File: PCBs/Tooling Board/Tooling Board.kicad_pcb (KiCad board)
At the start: 2 copper layers, 106 parts, among them J101 Screw Terminal, J102 Screw Terminal, J103 USB_B_Mini, J201 Conn_02x05_Odd_Even, J301 Conn_01x02, J302 Conn_01x02, J401 Screw Terminal, J402 Screw Terminal, J403 Screw Terminal, J404 Screw Terminal, J501 Screw Terminal, J502 Screw Terminal, J503 Screw Terminal, J504 Screw Terminal, J601 Screw Terminal, J602 Screw Terminal, J603 Screw Terminal, J604 Screw Terminal, J701 Conn_01x03, J702 Conn_01x04, J703 Conn_01x03, J801 Conn_01x02, Q301 Q_NMOS_DGS, Q302 Q_NMOS_DGS, SW201 SW_Push, U101 TLV733P, U201 ATSAMD21E18A-MFTCT-ND, U401 74LVC2G14, U402 LN298P, U501 74LVC2G14, U502 LN298P, U601 74LVC2G14, U602 LN298P, U701 ADA_IMU, U801 CA3140AM, U802 LM2776, U803 TL081BCDG4, Y201 32.7680kHz

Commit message: Removed 3rd DC Motor Driver
-Can only do 4 DC motors now, not enough board space
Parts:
- removed C601, C602: 100nF, Capacitors_SMD:C_0805_HandSoldering
- removed J601, J602, J603, J604: Screw Terminal, EER:RingTerminal
- removed R601, R602: 0.5, Resistors_SMD:R_1206_HandSoldering
- removed U601: 74LVC2G14, EER:PSON50P140X100X40-6N
- removed U602: LN298P, EER:POWER-SO20
- RV801: footprint Potentiometers:Potentiometer_Trimmer_Bourns_3269W -> Potentiometers:Potentiometer_Trimmer_Bourns_3296W
- moved J403 297.6 mm to (159.6, 47.4), turned to 90 degrees
- moved J404 297.6 mm to (159.6, 38.0), turned to 90 degrees
- moved U802 285.1 mm to (159.6, 97.0)
- moved J402 274.4 mm to (144.6, 38.0), turned to 90 degrees
- moved J401 274.2 mm to (144.4, 47.2), turned to 90 degrees
- moved U803 252.4 mm to (198.2, 69.4)
- moved SW201 252.0 mm to (145.8, 87.8), turned to 90 degrees
- moved Q302 249.9 mm to (188.0, 71.4)
- moved U801 249.4 mm to (197.6, 78.6)
- moved U201 244.1 mm to (149.5, 77.7)
- moved J201 242.2 mm to (151.2, 90.4), turned to 180 degrees
- moved Q301 217.9 mm to (158.4, 71.4)
- moved J502 210.4 mm to (133.2, 37.8), turned to 90 degrees
- moved J504 203.3 mm to (133.0, 47.0), turned to 90 degrees
- moved J102 202.4 mm to (132.4, 78.2), turned to 90 degrees
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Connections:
- U201 pad 25: DirA3 -> Net-(U201-Pad25)
- U201 pad 3: DirB3 -> Net-(U201-Pad3)
- U201 pad 7: EnableA3 -> Net-(U201-Pad7)
- U201 pad 8: EnableB3 -> Net-(U201-Pad8)
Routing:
- net (no net): vias 0 -> 3
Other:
- board outline added: 104.7 x 67.4 mm

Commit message: Almost Finished
-Still going, help
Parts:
- removed D801: GREEN, LEDs:LED_0805_HandSoldering
- removed R301, R302: 100k, Resistors_SMD:R_0805_HandSoldering
- removed R809: 1k, Resistors_SMD:R_0805_HandSoldering
- C103, C105, C106, C107, C201, C202, C203, C204, C207, C401, C402, C501, C502, C701, C801, C802, C803, C804, C805, C806, C807, C808, C809, C810, C811, C812, C813: footprint Capacitors_SMD:C_0805_HandSoldering -> Capacitors_SMD:C_0805
- C205, C206: footprint Capacitors_SMD:C_0603_HandSoldering -> Capacitors_SMD:C_0603
- D101, D201, D202: footprint LEDs:LED_0805_HandSoldering -> LEDs:LED_0805
- J301, J302, J801: footprint Junction Box:70553-02 -> EER:1x2_molex_llc_new
- J701, J703: footprint Junction Box:70553-03 -> EER:1x3_molex_llc
- J702: footprint Junction Box:70553-04 -> EER:1x4_molex_llc
- R101, R201, R202, R203, R204, R205, R701, R702, R703, R801, R802, R803, R804, R805, R806, R807, R808: footprint Resistors_SMD:R_0805_HandSoldering -> Resistors_SMD:R_0805
- R401, R402, R501, R502: footprint Resistors_SMD:R_1206_HandSoldering -> Resistors_SMD:R_1206
- moved C701 369.8 mm to (196.5, 71.8), turned to 270 degrees
- moved R701 369.4 mm to (196.4, 68.2), turned to 270 degrees
- moved R702 368.0 mm to (196.4, 65.1), turned to 270 degrees
- moved R204 365.2 mm to (194.5, 82.6), turned to 90 degrees
- moved R205 364.9 mm to (194.6, 78.1), turned to 270 degrees
- moved R402 351.7 mm to (182.5, 57.0), turned to 180 degrees
- moved C402 351.6 mm to (181.3, 66.8), turned to 270 degrees
- moved R703 347.1 mm to (189.1, 91.2), turned to 180 degrees
- moved J701 332.1 mm to (192.9, 99.2), turned to 90 degrees
- moved J702 328.8 mm to (197.3, 86.7)
- moved J703 319.8 mm to (197.5, 73.4)
- moved U401 314.1 mm to (165.7, 69.7), turned to 90 degrees
- moved C401 311.1 mm to (159.8, 63.0), turned to 270 degrees
- moved R401 308.0 mm to (159.8, 58.4), turned to 270 degrees
- moved C207 252.8 mm to (152.1, 68.0)
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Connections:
- C103 pad 1: +5V -> /MicroController/+5V_IN
- F101 pad 1: +5V -> /MicroController/+5V_IN
- L202 pad 2: +5V -> /MicroController/+5V_IN
- U101 pad 1: +5V -> /MicroController/+5V_IN
- U101 pad 3: +5V -> /MicroController/+5V_IN
- U201 pad 33: (no net) -> GND
- U701 pad 10: Net-(U701-Pad10) -> +3V3
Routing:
- net +3V3: track 0.00 -> 120.1 mm, vias 0 -> 6
- net GND: track 0.00 -> 100.9 mm, vias 0 -> 49
- net +5V: track 0.00 -> 97.1 mm, vias 0 -> 7
- net +12V: track 0.00 -> 87.0 mm, vias 0 -> 2
- net SCL: track 0.00 -> 64.5 mm, vias 0 -> 2
- net SDA: track 0.00 -> 64.3 mm, vias 0 -> 3
- net USB-: track 0.00 -> 57.3 mm, vias 0 -> 2
- net USB+: track 0.00 -> 54.1 mm, vias 0 -> 2
- net LED: track 0.00 -> 50.1 mm, vias 0 -> 2
- net T_DATA: track 0.00 -> 40.8 mm, vias 0 -> 2
- net DirA2: track 0.00 -> 39.8 mm, vias 0 -> 2
- net EnableA2: track 0.00 -> 39.1 mm, vias 0 -> 4
- net 3V3_FILT: track 0.00 -> 25.0 mm
- net -5V: track 0.00 -> 19.8 mm, vias 0 -> 4
- net Net-(R804-Pad1): track 0.00 -> 19.8 mm, vias 0 -> 4
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- added copper zone on F.Cu, net +12V
- added copper zone on F.Cu, net +3V3
- added copper zone on F.Cu, net +5V
- added copper zone on F.Cu, net -5V
- added copper zone on F.Cu, net /MicroController/+5V_IN
- added copper zone on F.Cu, net 3V3_FILT
- added copper zone on B.Cu, net GND
- added copper zone on F.Cu, net Net-(J301-Pad2)
- added copper zone on F.Cu, net Net-(J302-Pad2)
- added copper zone on F.Cu, net Net-(J401-Pad1)
- added copper zone on B.Cu, net Net-(J402-Pad1)
- added copper zone on F.Cu, net Net-(J403-Pad1)
- added copper zone on B.Cu, net Net-(J404-Pad1)
- added copper zone on F.Cu, net Net-(J501-Pad1)
- added copper zone on B.Cu, net Net-(J502-Pad1)
- added copper zone on F.Cu, net Net-(J503-Pad1)
- added copper zone on B.Cu, net Net-(J504-Pad1)
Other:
- net class Default: trace_width 0.25 -> 0.2; via_dia 0.8 -> 0.6; via_drill 0.4 -> 0.3
- rule via_min_size: 0.4 -> 0.3

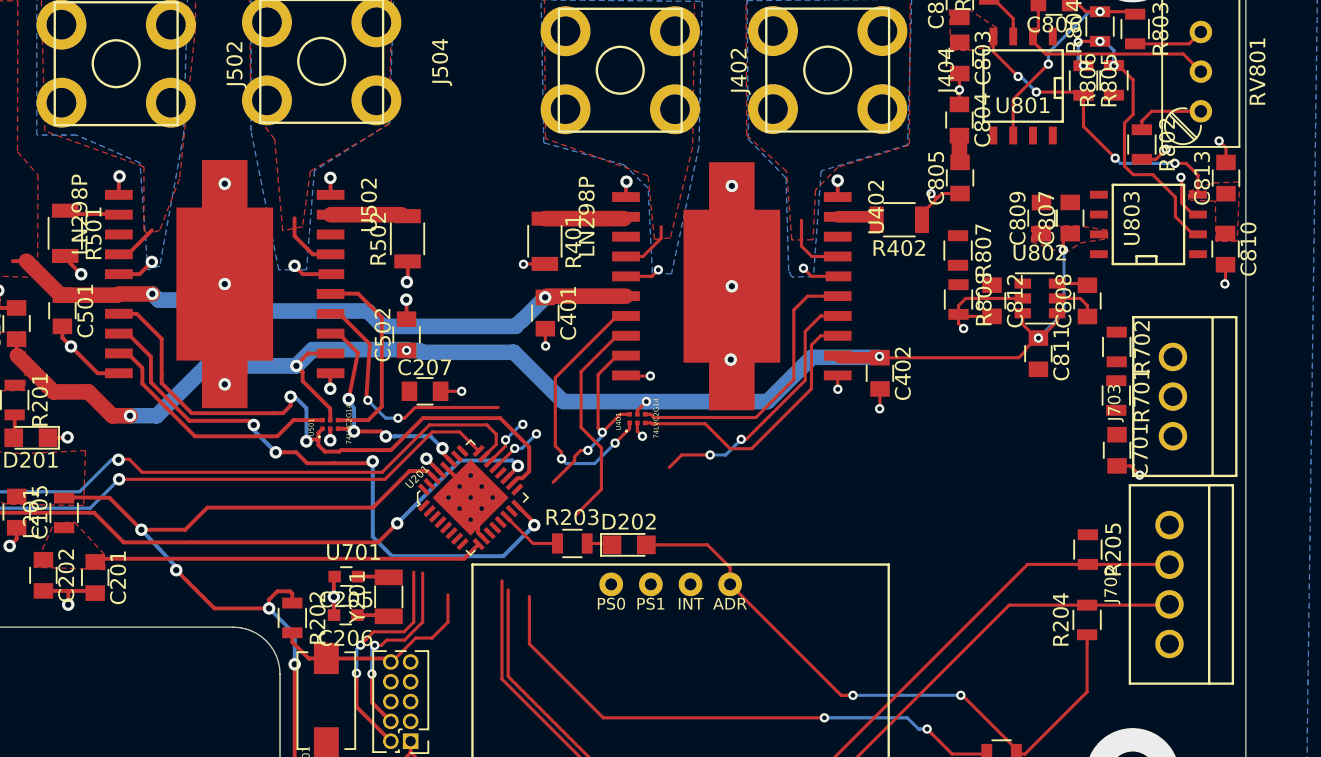
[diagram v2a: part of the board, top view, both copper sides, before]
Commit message: Just the Micro
-Need to fricken route the micro help
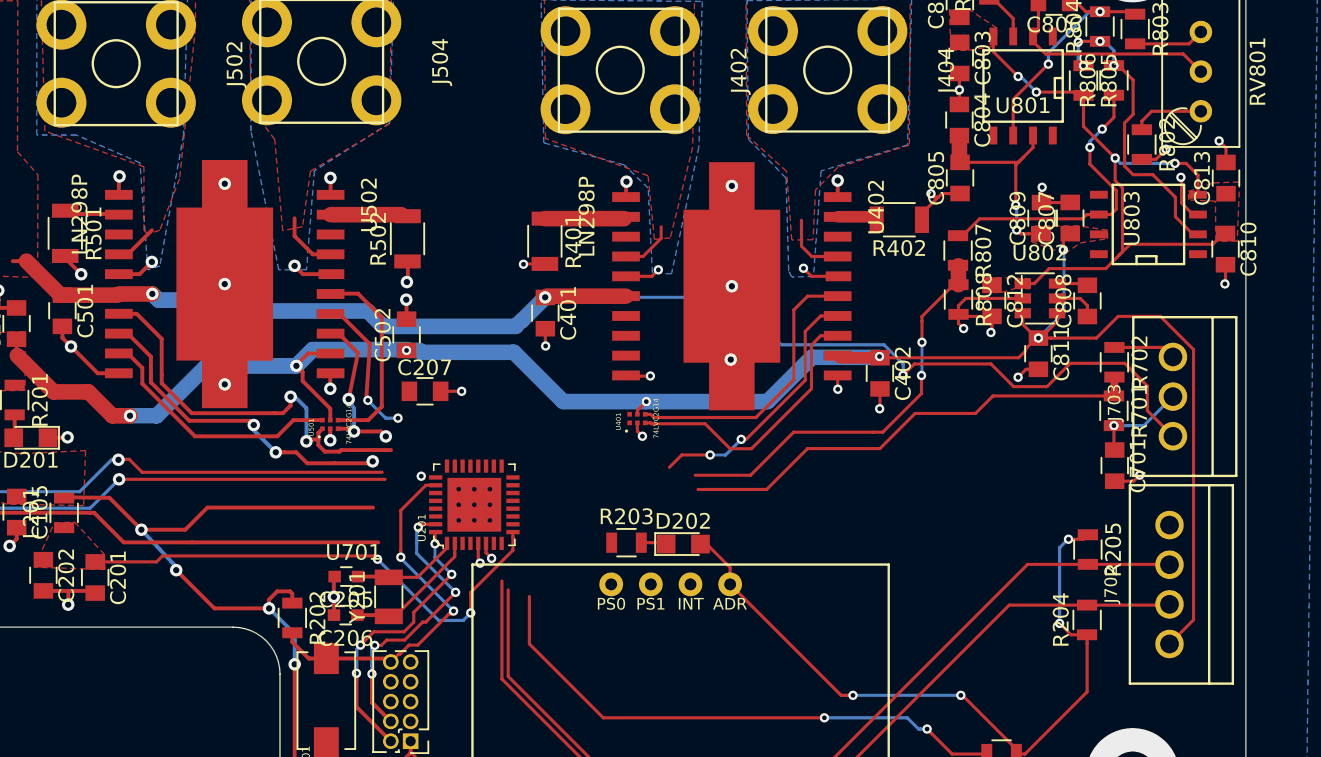
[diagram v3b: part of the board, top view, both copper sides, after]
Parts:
- moved D202 3.47 mm to (168.7, 77.8)
- moved R203 3.47 mm to (165.0, 77.7)
- moved R701 0.99 mm to (196.3, 69.2)
- moved R702 0.99 mm to (196.3, 66.1)
- moved C701 0.99 mm to (196.3, 72.7)
- turned U201 to 90 degrees
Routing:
- net +12V: track 87.0 -> 134.1 mm, vias 2 -> 3
- net +5V: track 97.1 -> 140.5 mm, vias 7 -> 9
- net V_METAL: track 0.00 -> 31.7 mm, vias 0 -> 1
- net V_PH: track 0.00 -> 27.2 mm, vias 0 -> 3
- net -5V: track 19.8 -> 40.7 mm
- net Net-(R806-Pad1): track 0.00 -> 19.5 mm, vias 0 -> 2
- net EnableA2: track 39.1 -> 20.9 mm, vias 4 -> 3
- net DirA1: track 17.3 -> 0.00 mm, vias 2 -> 0
- net EnableA1: track 14.2 -> 0.00 mm
- net DirA2: track 39.8 -> 26.4 mm
- net /Actuators/DCMotor1-2/Input2: track 13.1 -> 0.00 mm, vias 2 -> 0
- net LED: track 50.1 -> 37.7 mm, vias 2 -> 0
- net USB-: track 57.3 -> 46.8 mm
- net ~RESET~: track 13.9 -> 23.6 mm, vias 0 -> 2
- net USB+: track 54.1 -> 46.4 mm
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
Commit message: Finalized Tooling Board
woohoo!! Hopefully the chinese ppl get this guy approved quick so we avoid chinese new year
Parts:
- added U$12: EERLOGO, EER:EERLOGO, B.Cu at (192.3, 83.0)
- added U$15: MUNLOGO, EER:MUNLOGO, B.Cu at (192.5, 94.9)
- added U$16: MILOGO, EER:MILOGO, B.Cu at (174.4, 95.8)
- Q301: value Q_NMOS_DGS -> Q1
- moved C207 9.43 mm to (145.5, 74.7), turned to 180 degrees
- moved R402 1.58 mm to (181.6, 58.3), turned to 90 degrees
- moved U401 0.84 mm to (165.7, 70.6)
- moved J403 0.53 mm to (178.0, 37.6)
- moved J401 0.46 mm to (164.7, 37.5)
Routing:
- net +3V3: track 120.1 -> 150.0 mm, vias 8 -> 13
- net EnableA1: track 0.00 -> 19.3 mm, vias 0 -> 4
- net DirA1: track 0.00 -> 19.1 mm, vias 0 -> 2
- net SDA: track 60.7 -> 79.0 mm, vias 1 -> 0
- net V_METAL: track 31.7 -> 49.4 mm, vias 1 -> 2
- net SCL: track 61.1 -> 78.7 mm
- net V_PH: track 27.2 -> 43.6 mm, vias 3 -> 4
- net EnableA2: track 20.9 -> 37.2 mm, vias 3 -> 4
- net EnableB1: track 16.6 -> 28.6 mm, vias 2 -> 4
- net DirB1: track 17.7 -> 29.5 mm, vias 0 -> 2
- net DirA2: track 26.4 -> 38.2 mm, vias 2 -> 4
- net LED: track 37.7 -> 49.3 mm, vias 0 -> 2
- net T_DATA: track 40.8 -> 51.4 mm, vias 2 -> 4
- net Net-(R203-Pad1): track 0.00 -> 8.73 mm, vias 0 -> 2
- net EnableB2: track 9.37 -> 17.7 mm
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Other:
- board text added: "+12V"
- board text added: "+5V"
- board text added: "3V3"
- board text added: "Eastern Edge Robotics"
- board text added: "GND"
- board text added: "IMU"
- board text added: "LEDS"
- board text added: "M1+"
- board text added: "M1-"
- board text added: "M2+"
- board text added: "M2-"
- board text added: "M3+"
- board text added: "M3-"
- board text added: "M4+"
- board text added: "M4-"
- board text added: "MDETECT"
- board text added: "Mark Belbin - 2019"
- board text added: "PSENSE"
- board text added: "SCL"
- board text added: "SDA"
- board text added: "SWD"
- board text added: "TDATA"
- board text added: "TEMP"
- board text added: "Tooling Board"
- board text added: "V+"
- board text added: "V-"
- board text added: "VSEN"
- board text added: "pH IN"

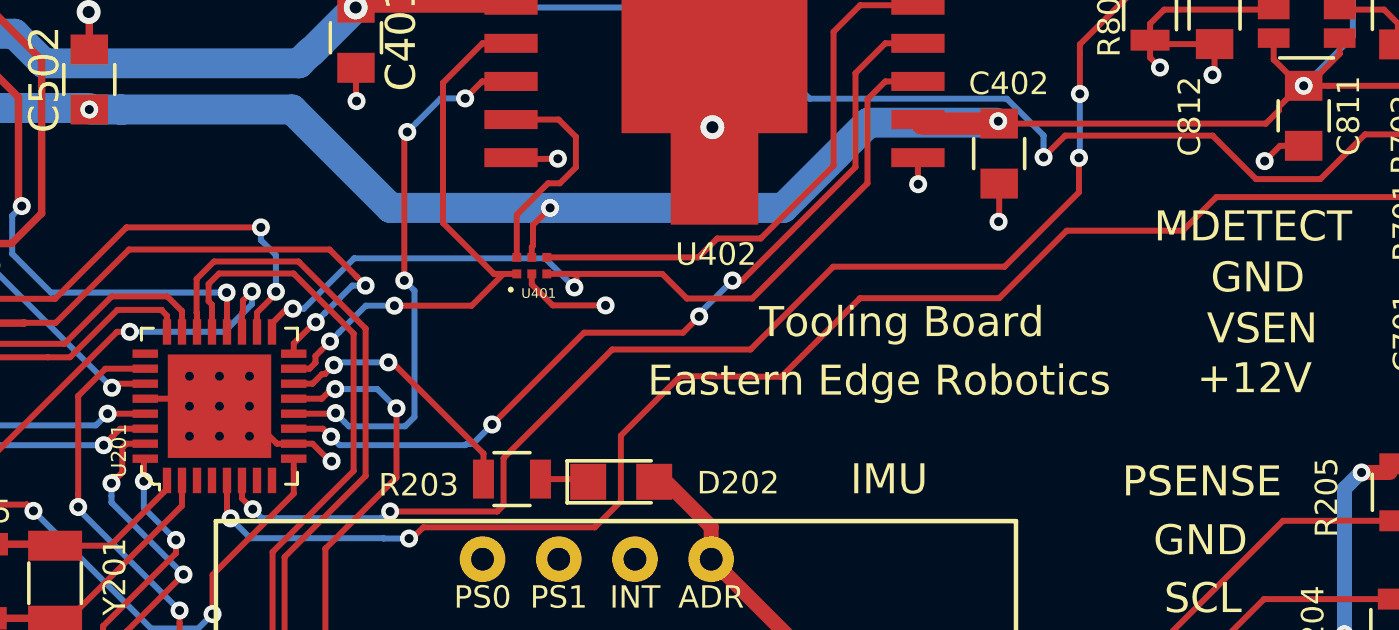
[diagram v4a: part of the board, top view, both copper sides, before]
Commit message: Tooling Board Finalized
-Checked Routing
-Added 3D models for all components
-She looks pretty good boys
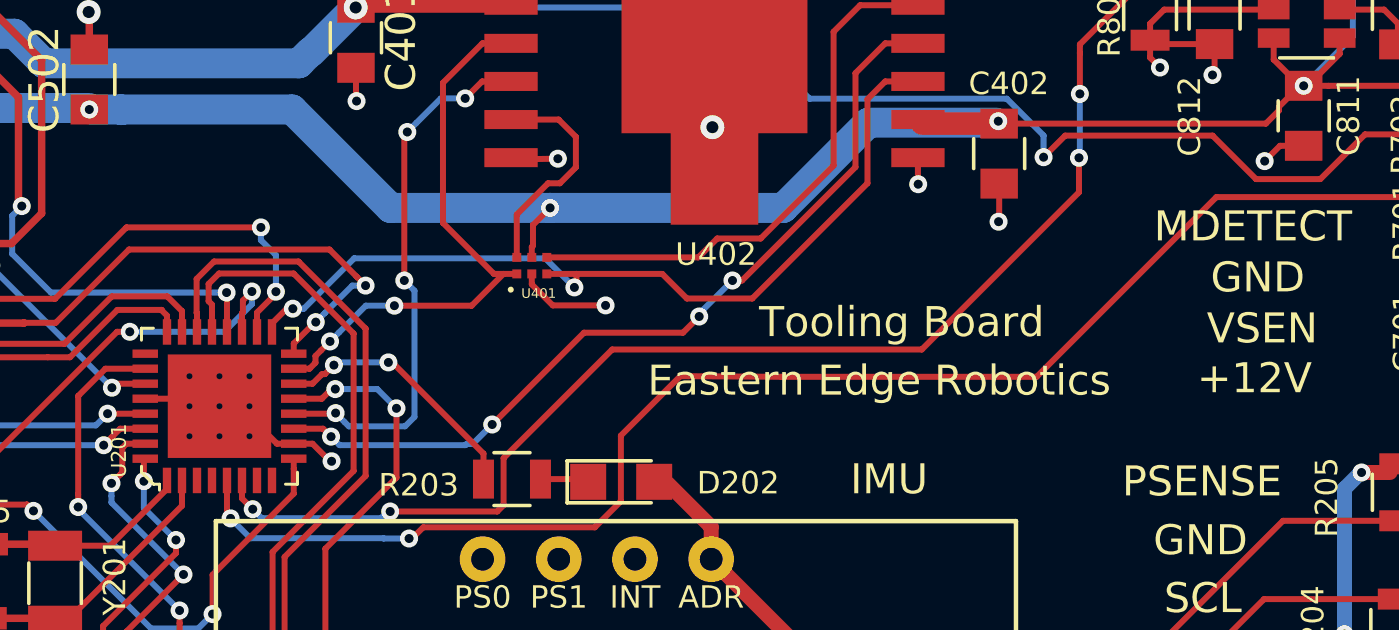
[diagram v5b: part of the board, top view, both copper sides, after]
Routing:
- net GND: track 113.1 -> 112.1 mm
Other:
- rule pad_to_mask_clearance: 0.2 -> 0.1

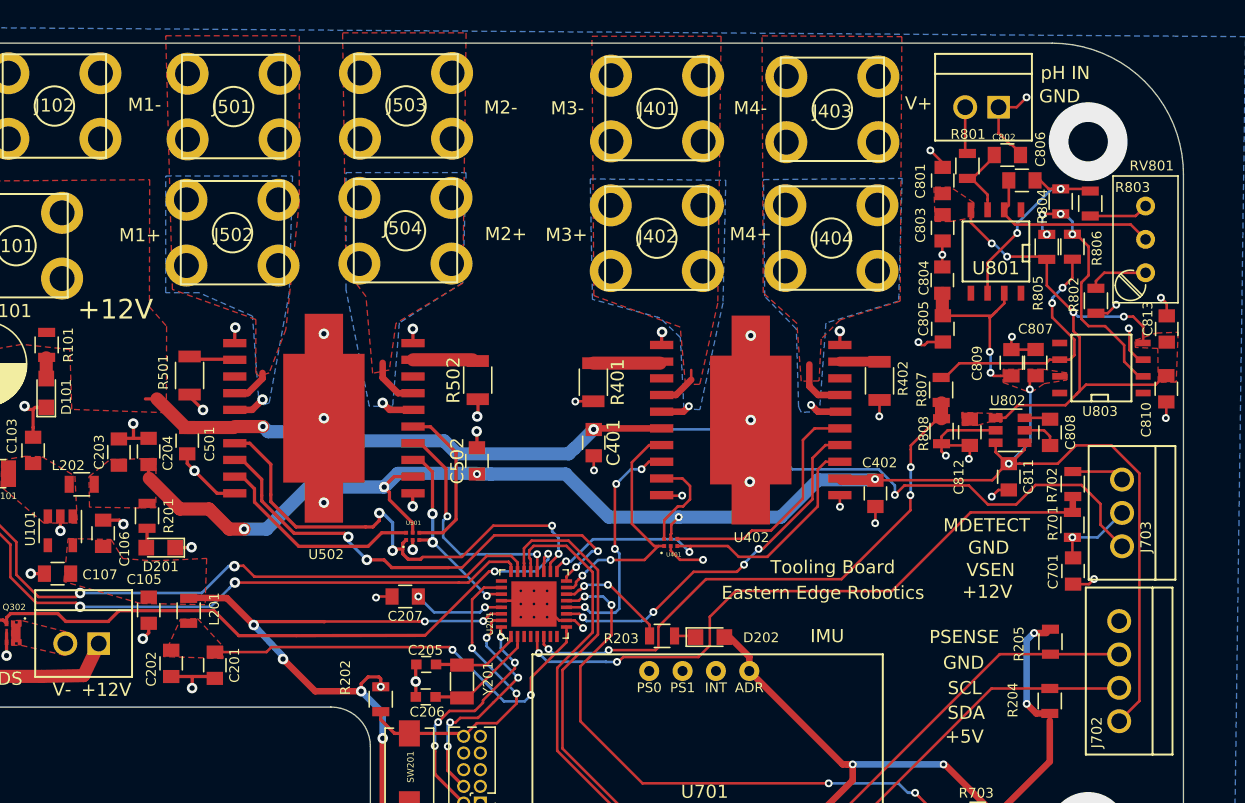
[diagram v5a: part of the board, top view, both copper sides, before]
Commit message: ToolingBoard Touch-ups
-Cleaned up routing
-Enlarged power traces
-Fixed return paths on motor ground
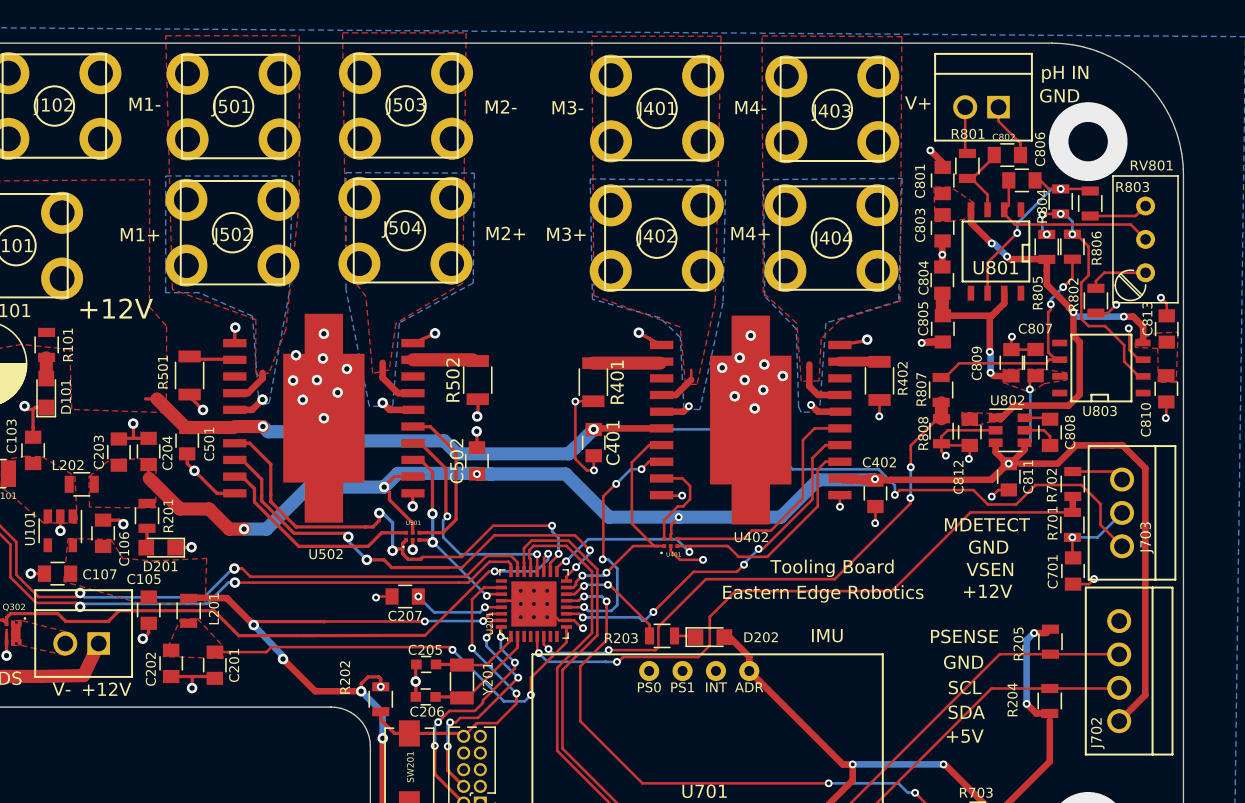
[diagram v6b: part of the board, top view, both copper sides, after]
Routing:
- net GND: track 112.1 -> 134.8 mm, vias 54 -> 65
- net -5V: track 40.7 -> 33.6 mm
- net +5V: track 141.5 -> 144.8 mm
- net EnableA2: track 37.2 -> 36.2 mm
- net Net-(R806-Pad1): track 19.5 -> 18.5 mm
- net EnableA1: track 19.3 -> 19.9 mm
